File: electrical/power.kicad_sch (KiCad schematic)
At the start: 0 parts

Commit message: #18 Adding decoupling capacitor.
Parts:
- added BT1: Battery_Cell, SMTU2032-C:SMTU2032C, symbol Device:Battery_Cell
- added C1: C, 0603YD106MAT2A:CAPC1608X90N, symbol Device:C
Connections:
- new net +3V0: BT1.1 (+), C1.2
- new net GND: BT1.2 (-), C1.1

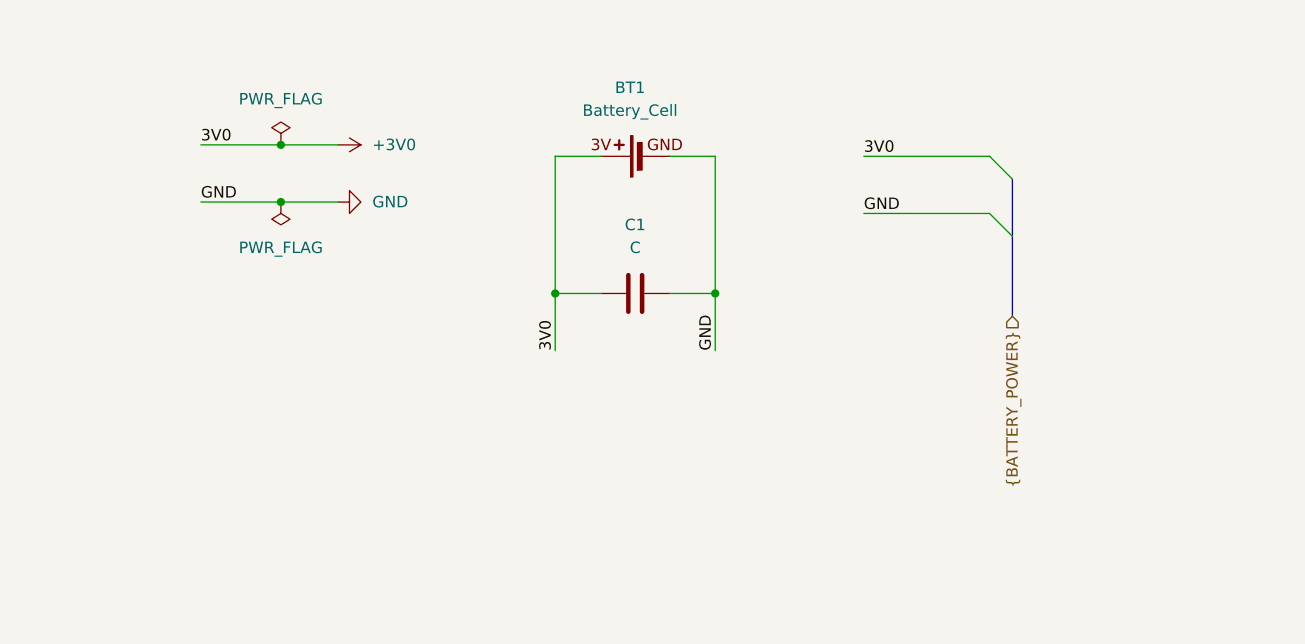
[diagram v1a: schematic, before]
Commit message: #3 Making minor changes to power.
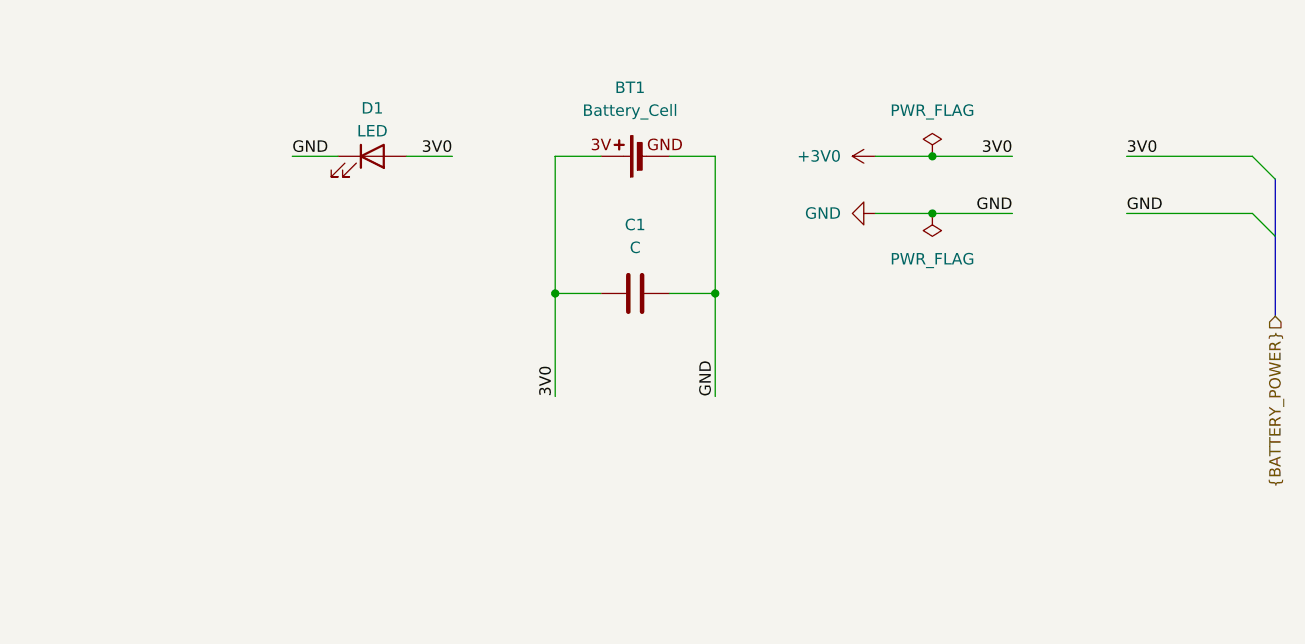
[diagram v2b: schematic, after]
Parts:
- added D1: LED, KT_EELP41.12-S2U1-25-2X4X-5-R18:KTEELP4112S2U1252X4X5R18, symbol Device:LED
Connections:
- net +3V0: now also D1.2 (A)
- net GND: now also D1.1 (K)

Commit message: #3 Implementing base schematic for processor.
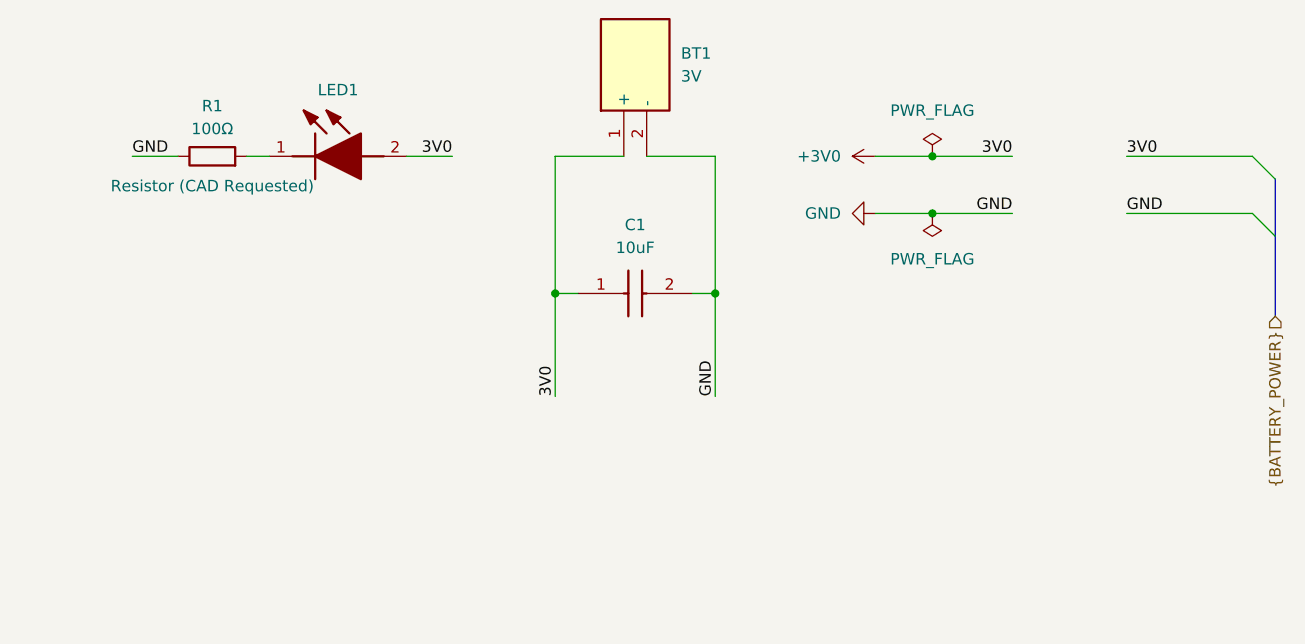
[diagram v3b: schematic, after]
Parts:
- removed BT1: Battery_Cell, SMTU2032-C:SMTU2032C, symbol Device:Battery_Cell
- removed C1: C, 0603YD106MAT2A:CAPC1608X90N, symbol Device:C
- removed D1: LED, KT_EELP41.12-S2U1-25-2X4X-5-R18:KTEELP4112S2U1252X4X5R18, symbol Device:LED
- added BT1: 3V, SMTU2032C, symbol SamacSys_Parts:SMTU2032-C
- added C1: 10uF, CAPC1608X90N, symbol SamacSys_Parts:0603YD106MAT2A
- added LED1: KT_EELP41.12-S2U1-25-2X4X-5-R18, KTEELP4112S2U1252X4X5R18, symbol SamacSys_Parts:KT_EELP41.12-S2U1-25-2X4X-5-R18
- added R1: 100Ω, symbol Device:R
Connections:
- net +3V0: now also BT1.1 (+), C1.1, LED1.2 (A)
- net GND: now also BT1.2 (-), C1.2, R1.1
- new net: LED1.1 (K), R1.2
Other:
- company: (none) -> AlumaPower
- title: (none) -> Etchasketch - Power

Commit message: #3 Updating schematic.
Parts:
- removed R1: 100Ω, symbol Device:R
- added R1: 100 Ω, SamacSys_Parts:RT73F1J100RBTD, symbol SamacSys_Parts:RT73F1J100RBTD
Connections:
- net GND: now also R1.1
- net at LED1.1 (K): now also R1.2
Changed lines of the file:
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@@
 	(wire
 		(pts
-			(xy 85.09 80.01) (xy 90.17 80.01)
+			(xy 74.93 80.01) (xy 80.01 80.01)
 		)
 		(stroke
@@
 	)
 	(label "GND"
-		(at 85.09 80.01 0)
+		(at 74.93 80.01 0)
 		(effects
 			(font
@@
 	)
 	(hierarchical_label "{BATTERY_POWER}"
-		(shape input)
+		(shape passive)
 		(at 212.09 97.79 270)
 		(effects
@@
 	)
 	(symbol
-		(lib_id "Device:R")
-		(at 93.98 80.01 90)
-		(unit 1)
-		(exclude_from_sim no)
-		(in_bom yes)
-		(on_board yes)
-		(dnp no)
-		(property "Reference" "R1"
-			(at 93.98 74.422 90)
-			(effects
-				(font
-					(size 1.27 1.27)
-				)
-			)
-		)
-		(property "Value" "100Ω"
-			(at 93.98 76.962 90)
-			(effects
-				(font
-					(size 1.27 1.27)
-				)
-			)
-		)
-		(property "Footprint" ""
-			(at 93.98 81.788 90)
-			(effects
-				(font
-					(size 1.27 1.27)
-				)
-				(hide yes)
-			)
-		)
-		(property "Datasheet" "https://www.te.com/commerce/DocumentDelivery/DDEController?Action=showdoc&DocId=Data+Sheet%7F1773450%7FA1%7Fpdf%7FEnglish%7FENG_DS_1773450_A1.pdf%7FCAT-F52-R"
-			(at 93.98 80.01 0)
-			(effects
-				(font
-					(size 1.27 1.27)
-				)
-				(hide yes)
-			)
-		)
-		(property "Description" "Resistor (CAD Requested)"
-			(at 93.98 83.312 90)
-			(effects
-				(font
-					(size 1.27 1.27)
-				)
-			)
-		)
-		(pin "1"
-		)
-		(pin "2"
-		)
-		(instances
-			(project ""
-				(path "/0ea7de92-e138-4a6c-b193-fca6869c3a12/ba769e44-f8cf-4eba-a81c-896c4be00b00"
-					(reference "R1")
-					(unit 1)
-				)
-			)
-		)
-	)
-	(symbol
 		(lib_id "power:PWR_FLAG")
 		(at 173.99 80.01 0)
@@
 					(unit 1)
 				)
+			)
+		)
+	)
+	(symbol
+		(lib_id "SamacSys_Parts:RT73F1J100RBTD")
+		(at 80.01 80.01 0)
+		(unit 1)
+		(exclude_from_sim no)
+		(in_bom yes)
+		(on_board yes)
+		(dnp no)
+		(fields_autoplaced yes)
+		(property "Reference" "R1"
+			(at 88.9 73.66 0)
+			(effects
+				(font
+					(size 1.27 1.27)
+				)
+			)
+		)
+		(property "Value" "100 Ω"
+			(at 88.9 76.2 0)
+			(effects
+				(font
+					(size 1.27 1.27)
+				)
+			)
+		)
+		(property "Footprint" "SamacSys_Parts:RT73F1J100RBTD"
+			(at 93.98 176.2 0)
+			(effects
+				(font
+					(size 1.27 1.27)
+				)
+				(justify left top)
+				(hide yes)
+			)
+		)
+		(property "Datasheet" "https://www.te.com/commerce/DocumentDelivery/DDEController?Action=srchrtrv&DocNm=1773450&DocType=Data%20Sheet&DocLang=English&DocFormat=pdf&PartCntxt=9-2176757-7"
+			(at 93.98 276.2 0)
+			(effects
+				(font
+					(size 1.27 1.27)
+				)
+				(justify left top)
+				(hide yes)
+			)
+		)
+		(property "Description" "SMD Chip Resistor, 100 ohm, +/- 0.1%, 200 mW, 0603 [1608 Metric], Thick Film, High Precision"
+			(at 80.01 80.01 0)
+			(effects
+				(font
+					(size 1.27 1.27)
+				)
+				(hide yes)
+			)
+		)
+		(property "Height" "0.55"
+			(at 93.98 476.2 0)
+			(effects
+				(font
+					(size 1.27 1.27)
+				)
+				(justify left top)
+				(hide yes)
+			)
+		)
+		(property "Mouser Part Number" ""
+			(at 93.98 576.2 0)
+			(effects
+				(font
+					(size 1.27 1.27)
+				)
+				(justify left top)
+				(hide yes)
+			)
+		)
+		(property "Mouser Price/Stock" ""
+			(at 93.98 676.2 0)
+			(effects
+				(font
+					(size 1.27 1.27)
+				)
+				(justify left top)
+				(hide yes)
+			)
+		)
+		(property "Manufacturer_Name" "TE Connectivity"
+			(at 93.98 776.2 0)
+			(effects
+				(font
+					(size 1.27 1.27)
+				)
+				(justify left top)
+				(hide yes)
+			)
+		)
+		(property "Manufacturer_Part_Number" "RT73F1J100RBTD"
+			(at 93.98 876.2 0)
+			(effects
+				(font
+					(size 1.27 1.27)
+				)
+				(justify left top)
+				(hide yes)
+			)
+		)
+		(pin "1"
+		)
+		(pin "2"
+		)
+		(instances
+			(project ""
+				(path "/0ea7de92-e138-4a6c-b193-fca6869c3a12/ba769e44-f8cf-4eba-a81c-896c4be00b00"
+					(reference "R1")
+					(unit 1)
+				)

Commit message: #17 Making layout. Errors rpesent.
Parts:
- BT1: footprint SMTU2032C -> SamacSys_Parts:SMTU2032C
- C1: footprint CAPC1608X90N -> SamacSys_Parts:CAPC1608X90N
- LED1: footprint KTEELP4112S2U1252X4X5R18 -> SamacSys_Parts:KTEELP4112S2U1252X4X5R18
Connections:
- net +3V0 renamed 3V0
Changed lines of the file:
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@@
-		(color 0 0 0 0)
-	)
-	(junction
-		(at 173.99 80.01)
-		(diameter 0)
-		(color 0 0 0 0)
-	)
-	(junction
-		(at 173.99 86.36)
-		(diameter 0)
 		(color 0 0 0 0)
 	)
@@
 	(wire
 		(pts
-			(xy 74.93 80.01) (xy 80.01 80.01)
+			(xy 72.39 80.01) (xy 80.01 80.01)
 		)
 		(stroke
@@
 	(wire
 		(pts
-			(xy 173.99 86.36) (xy 167.64 86.36)
-		)
-		(stroke
-			(width 0)
-			(type default)
-		)
-	)
-	(wire
-		(pts
 			(xy 132.08 80.01) (xy 139.7 80.01)
 		)
@@
 	(wire
 		(pts
-			(xy 115.57 80.01) (xy 120.65 80.01)
+			(xy 115.57 80.01) (xy 124.46 80.01)
 		)
 		(stroke
@@
 		(pts
 			(xy 97.79 80.01) (xy 100.33 80.01)
-		)
-		(stroke
-			(width 0)
-			(type default)
-		)
-	)
-	(wire
-		(pts
-			(xy 173.99 80.01) (xy 167.64 80.01)
 		)
 		(stroke
@@
 	)
 	(label "GND"
-		(at 74.93 80.01 0)
+		(at 72.39 80.01 0)
 		(effects
 			(font
@@
 	)
 	(label "3V0"
-		(at 120.65 80.01 180)
+		(at 124.46 80.01 180)
 		(effects
 			(font
@@
 			)
 		)
-		(property "Footprint" "SMTU2032C"
+		(property "Footprint" "SamacSys_Parts:SMTU2032C"
 			(at 234.62 63.5 0)
 			(effects
@@
 			)
 		)
-		(property "Footprint" "CAPC1608X90N"
+		(property "Footprint" "SamacSys_Parts:CAPC1608X90N"
 			(at 143.51 191.44 0)
 			(effects
@@
 				(path "/0ea7de92-e138-4a6c-b193-fca6869c3a12/ba769e44-f8cf-4eba-a81c-896c4be00b00"
 					(reference "C1")
-					(unit 1)
-				)
-			)
-		)
-	)
-	(symbol
-		(lib_id "power:GND")
-		(at 167.64 86.36 270)
-		(mirror x)
-		(unit 1)
-		(exclude_from_sim no)
-		(in_bom yes)
-		(on_board yes)
-		(dnp no)
-		(fields_autoplaced yes)
-		(property "Reference" "#PWR01"
-			(at 161.29 86.36 0)
-			(effects
-				(font
-					(size 1.27 1.27)
-				)
-				(hide yes)
-			)
-		)
-		(property "Value" "GND"
-			(at 163.83 86.3599 90)
-			(effects
-				(font
-					(size 1.27 1.27)
-				)
-				(justify right)
-			)
-		)
-		(property "Footprint" ""
-			(at 167.64 86.36 0)
-			(effects
-				(font
-					(size 1.27 1.27)
-				)
-				(hide yes)
-			)
-		)
-		(property "Datasheet" ""
-			(at 167.64 86.36 0)
-			(effects
-				(font
-					(size 1.27 1.27)
-				)
-				(hide yes)
-			)
-		)
-		(property "Description" "Power symbol creates a global label with name \"GND\" , ground"
-			(at 167.64 86.36 0)
-			(effects
-				(font
-					(size 1.27 1.27)
-				)
-				(hide yes)
-			)
-		)
-		(pin "1"
-		)
-		(instances
-			(project ""
-				(path "/0ea7de92-e138-4a6c-b193-fca6869c3a12/ba769e44-f8cf-4eba-a81c-896c4be00b00"
-					(reference "#PWR01")
-					(unit 1)
-				)
-			)
-		)
-	)
-	(symbol
-		(lib_id "power:+3V0")
-		(at 167.64 80.01 90)
-		(mirror x)
-		(unit 1)
-		(exclude_from_sim no)
-		(in_bom yes)
-		(on_board yes)
-		(dnp no)
-		(fields_autoplaced yes)
-		(property "Reference" "#PWR02"
-			(at 171.45 80.01 0)
-			(effects
-				(font
-					(size 1.27 1.27)
-				)
-				(hide yes)
-			)
-		)
-		(property "Value" "+3V0"
-			(at 163.83 80.0099 90)
-			(effects
-				(font
-					(size 1.27 1.27)
-				)
-				(justify left)
-			)
-		)
-		(property "Footprint" ""
-			(at 167.64 80.01 0)
-			(effects
-				(font
-					(size 1.27 1.27)
-				)
-				(hide yes)
-			)
-		)
-		(property "Datasheet" ""
-			(at 167.64 80.01 0)
-			(effects
-				(font
-					(size 1.27 1.27)
-				)
-				(hide yes)
-			)
-		)
-		(property "Description" "Power symbol creates a global label with name \"+3V0\""
-			(at 167.64 80.01 0)
-			(effects
-				(font
-					(size 1.27 1.27)
-				)
-				(hide yes)
-			)
-		)
-		(pin "1"
-		)
-		(instances
-			(project ""
-				(path "/0ea7de92-e138-4a6c-b193-fca6869c3a12/ba769e44-f8cf-4eba-a81c-896c4be00b00"
-					(reference "#PWR02")
 					(unit 1)
 				)
@@
 			)
 		)
-		(property "Footprint" "KTEELP4112S2U1252X4X5R18"
+		(property "Footprint" "SamacSys_Parts:KTEELP4112S2U1252X4X5R18"
 			(at 113.03 173.66 0)
 			(effects

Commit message: Making progress on schematic and developing IOC.
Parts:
- removed BT1: 3V, SamacSys_Parts:SMTU2032C, symbol SamacSys_Parts:SMTU2032-C
- removed C1: 10uF, SamacSys_Parts:CAPC1608X90N, symbol SamacSys_Parts:0603YD106MAT2A
- removed LED1: KT_EELP41.12-S2U1-25-2X4X-5-R18, SamacSys_Parts:KTEELP4112S2U1252X4X5R18, symbol SamacSys_Parts:KT_EELP41.12-S2U1-25-2X4X-5-R18
- removed R1: 100 Ω, SamacSys_Parts:RT73F1J100RBTD, symbol SamacSys_Parts:RT73F1J100RBTD
- added BT1, BT2: +3V0, symbol adrians_favs:SMD_BATTERY_SINGLE_CELL_CR2032
- added D1: Green, adrians_favs:SMD_LED_GREEN_0603, symbol adrians_favs:SMD_LED_GREEN_0603_2P5V
- added R1: 110R, adrians_favs:SMD_RESISTOR_0603, symbol adrians_favs:SMD_RESISTOR_0603_110R
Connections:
- net GND: now also BT1.2 (-), BT2.2 (-), R1.1
- new net: D1.1 (K), R1.2
- new net +3V0: BT1.1 (+), BT2.1 (+), D1.2 (A)
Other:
- company: AlumaPower -> (none)
- title: Etchasketch - Power -> (none)

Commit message: Adding user input.
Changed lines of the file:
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@@
 	)
 	(global_label "GND"
-		(shape input)
+		(shape passive)
 		(at 180.34 110.49 90)
 		(fields_autoplaced yes)
@@
 		)
 		(property "Intersheetrefs" "${INTERSHEET_REFS}"
-			(at 180.34 103.6343 90)
+			(at 180.34 104.7456 90)
 			(effects
 				(font
@@
 	)
 	(global_label "+3V0"
-		(shape input)
+		(shape passive)
 		(at 165.1 110.49 90)
 		(fields_autoplaced yes)
@@
 		)
 		(property "Intersheetrefs" "${INTERSHEET_REFS}"
-			(at 165.1 102.4248 90)
+			(at 165.1 103.5361 90)
 			(effects
 				(font

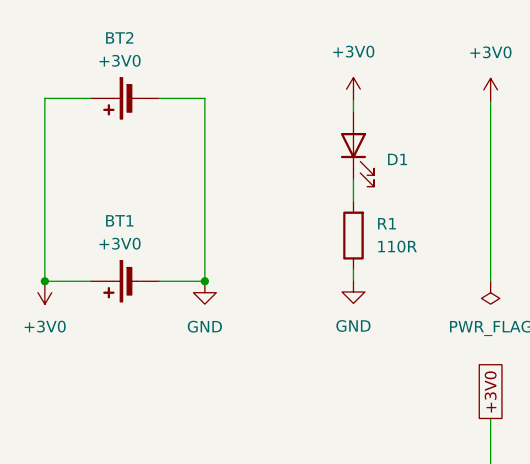
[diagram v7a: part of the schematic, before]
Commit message: Adding decoupling capacitors for STM.
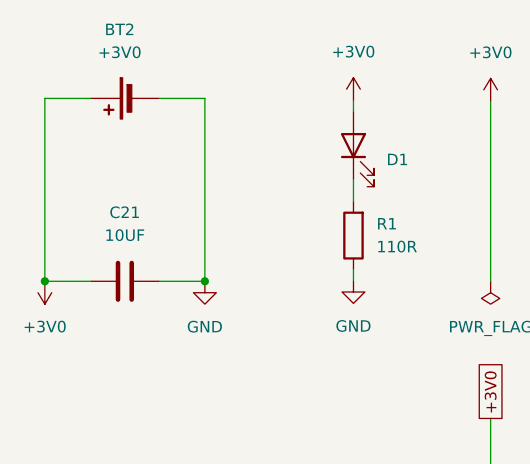
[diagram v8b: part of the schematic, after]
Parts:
- removed BT1: +3V0, symbol adrians_favs:SMD_BATTERY_SINGLE_CELL_CR2032
- added C21: 10UF, adrians_favs:SMD_CAPACITOR_CERAMIC_0603, symbol adrians_favs:SMD_CAPACITOR_CERAMIC_0603_10UF
- BT2: footprint (none) -> adrians_favs:SMD_BATTERY_SINGLE_CELL_CR2032; Store (none) -> https://mou.sr/4rY7KUn
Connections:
- net +3V0: now also C21.1
- net GND: now also C21.2
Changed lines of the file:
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@@
+	)
+	(symbol
+		(lib_id "adrians_favs:SMD_CAPACITOR_CERAMIC_0603_10UF")
+		(at 124.46 95.25 90)
+		(unit 1)
+		(exclude_from_sim no)
+		(in_bom yes)
+		(on_board yes)
+		(dnp no)
+		(fields_autoplaced yes)
+		(property "Reference" "C21"
+			(at 124.46 87.63 90)
+			(effects
+				(font
+					(size 1.27 1.27)
+				)
+			)
+		)
+		(property "Value" "10UF"
+			(at 124.46 90.17 90)
+			(effects
+				(font
+					(size 1.27 1.27)
+				)
+			)
+		)
+		(property "Footprint" "adrians_favs:SMD_CAPACITOR_CERAMIC_0603"
+			(at 128.27 94.2848 0)
+			(effects
+				(font
+					(size 1.27 1.27)
+				)
+				(hide yes)
+			)
+		)
+		(property "Datasheet" "https://datasheets.kyocera-avx.com/cx5r.pdf"
+			(at 124.46 95.25 0)
+			(effects
+				(font
+					(size 1.27 1.27)
+				)
+				(hide yes)
+			)
+		)
+		(property "Description" "10uF ceramic capacitor in 0603 form-factor."
+			(at 124.46 95.25 0)
+			(effects
+				(font
+					(size 1.27 1.27)
+				)
+				(hide yes)
+			)
+		)
+		(property "Store" "https://mou.sr/49dVOXa"
+			(at 124.46 95.25 0)
+			(effects
+				(font
+					(size 1.27 1.27)
+				)
+				(hide yes)
+			)
+		)
+		(pin "1"
+		)
+		(pin "2"
+		)
+		(instances
+			(project ""
+				(path "/677117a5-2713-4117-9fd9-f2791321eb47/a868c076-ff46-444b-a86b-c9ac10004481"
+					(reference "C21")
+					(unit 1)
+				)
+			)
+		)
 	)
 	(symbol
@@
 		(fields_autoplaced yes)
 		(property "Reference" "BT2"
-			(at 123.8885 68.26 0)
+			(at 123.8885 67.31 0)
 			(effects
 				(font
@@
 		)
 		(property "Value" "+3V0"
-			(at 123.8885 70.8 0)
-			(effects
-				(font
-					(size 1.27 1.27)
-				)
-			)
-		)
-		(property "Footprint" ""
+			(at 123.8885 69.85 0)
+			(effects
+				(font
+					(size 1.27 1.27)
+				)
+			)
+		)
+		(property "Footprint" "adrians_favs:SMD_BATTERY_SINGLE_CELL_CR2032"
 			(at 124.46 76.454 90)
 			(effects
@@
 			)
 		)
-		(property "Datasheet" "~"
+		(property "Datasheet" "https://www.renata.com/en/"
 			(at 124.206 74.93 0)
 			(effects
@@
 			)
 		)
-		(property "Description" "Single-cell battery"
+		(property "Description" "Signle cell battery case for a CR2032 coincell battery."
 			(at 125.73 74.93 90)
+			(effects
+				(font
+					(size 1.27 1.27)
+				)
+				(hide yes)
+			)
+		)
+		(property "Store" "https://mou.sr/4rY7KUn"
+			(at 124.46 74.93 0)
 			(effects
 				(font
@@
 					(unit 1)
 				)
-			)
-		)
-	)
-	(symbol
-		(lib_id "adrians_favs:SMD_BATTERY_SINGLE_CELL_CR2032")
-		(at 124.46 95.25 0)
-		(mirror x)
-		(unit 1)
-		(exclude_from_sim no)
-		(in_bom yes)
-		(on_board yes)
-		(dnp no)
-		(fields_autoplaced yes)
-		(property "Reference" "BT1"
-			(at 123.8885 88.58 0)
-			(effects
-				(font
-					(size 1.27 1.27)
-				)
-			)
-		)
-		(property "Value" "+3V0"
-			(at 123.8885 91.12 0)
-			(effects
-				(font
-					(size 1.27 1.27)
-				)
-			)
-		)
-		(property "Footprint" ""
-			(at 124.46 96.774 90)
-			(effects
-				(font
-					(size 1.27 1.27)
-				)
-				(hide yes)
-			)
-		)
-		(property "Datasheet" "~"
-			(at 124.206 95.25 0)
-			(effects
-				(font
-					(size 1.27 1.27)
-				)
-				(hide yes)
-			)
-		)
-		(property "Description" "Single-cell battery"
-			(at 125.73 95.25 90)
-			(effects
-				(font
-					(size 1.27 1.27)
-				)
-				(hide yes)
-			)
-		)
-		(pin "2"
-		)
-		(pin "1"
-		)
-		(instances
-			(project "electrical"
-				(path "/677117a5-2713-4117-9fd9-f2791321eb47/a868c076-ff46-444b-a86b-c9ac10004481"
-					(reference "BT1")
-					(unit 1)
-				)
